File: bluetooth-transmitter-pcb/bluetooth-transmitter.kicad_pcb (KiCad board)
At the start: 2 copper layers, 16 parts, among them J1 Boot option, J2 Flash UART, SW1 Reset, SW2 RotaryEncoder_Switch, U1 ESP32-WROOM-32

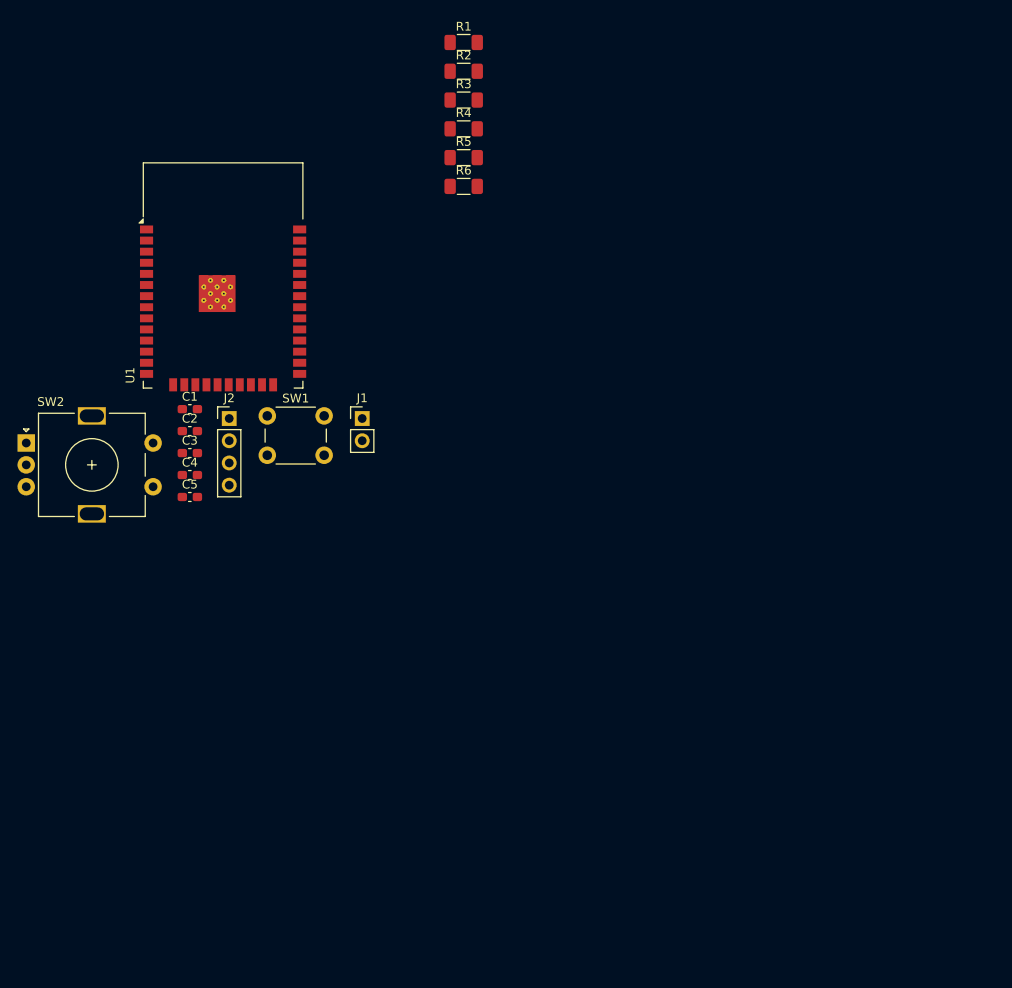
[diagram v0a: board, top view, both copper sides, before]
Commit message: Update PCB to last version
Add power chain and PCM1808 to schematic. Create PCB from shecmatic.
Make PCB ready for production.
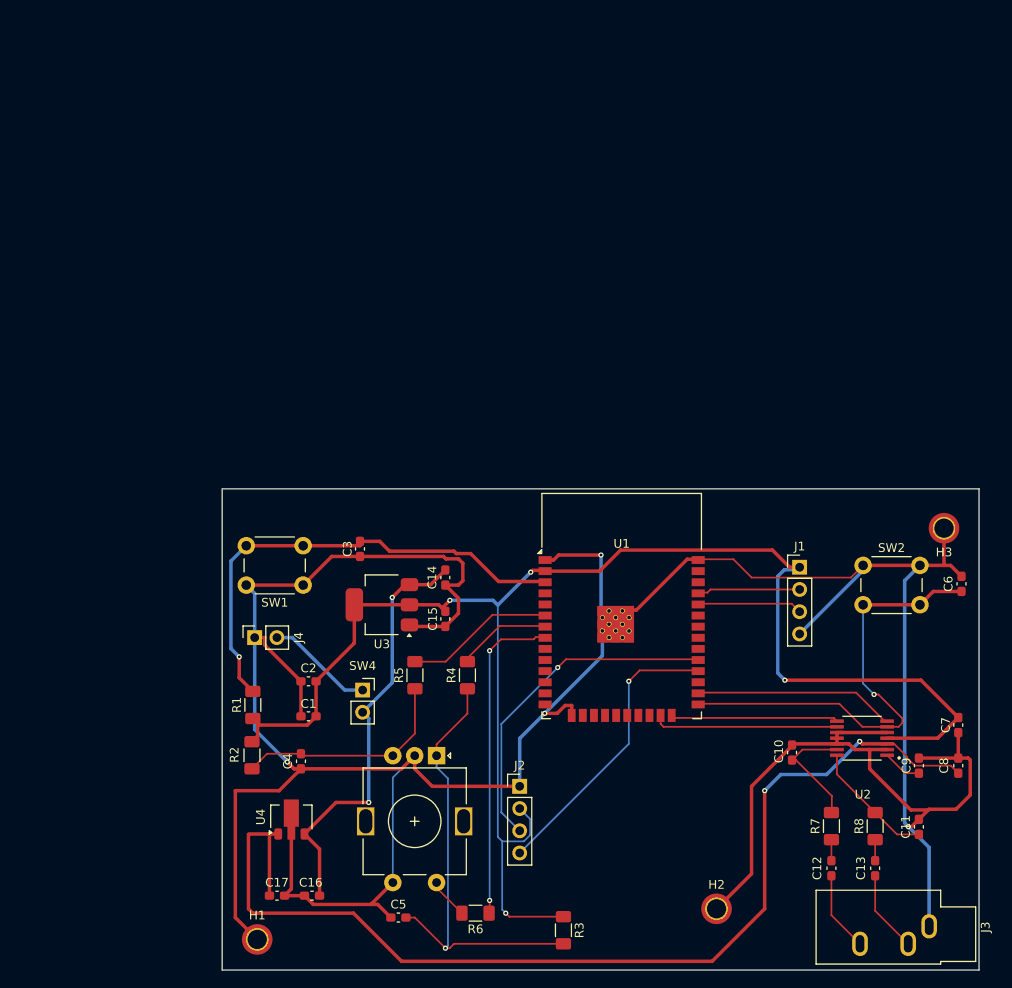
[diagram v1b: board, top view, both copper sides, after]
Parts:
- added C10: 2200pF, Capacitor_SMD:C_0603_1608Metric_Pad1.08x0.95mm_HandSolder, F.Cu at (128.6, 99.1)
- added C11: 2200pF, Capacitor_SMD:C_0603_1608Metric_Pad1.08x0.95mm_HandSolder, F.Cu at (143.1, 107.6)
- added C12: 2.2uF, Capacitor_SMD:C_0603_1608Metric_Pad1.08x0.95mm_HandSolder, F.Cu at (133.1, 112.4)
- added C13: 2.2uF, Capacitor_SMD:C_0603_1608Metric_Pad1.08x0.95mm_HandSolder, F.Cu at (138.1, 112.4)
- added C14: 1uF, Capacitor_SMD:C_0603_1608Metric_Pad1.08x0.95mm_HandSolder, F.Cu at (89.0, 79.1)
- added C15: 1uF, Capacitor_SMD:C_0603_1608Metric_Pad1.08x0.95mm_HandSolder, F.Cu at (89.0, 83.9)
- added C16: 0.1uF, Capacitor_SMD:C_0603_1608Metric_Pad1.08x0.95mm_HandSolder, F.Cu at (73.8, 115.5)
- added C17: 0.1uF, Capacitor_SMD:C_0603_1608Metric_Pad1.08x0.95mm_HandSolder, F.Cu at (69.8, 115.5)
- added C6: 1uF, Capacitor_SMD:C_0603_1608Metric_Pad1.08x0.95mm_HandSolder, F.Cu at (148.0, 79.9)
- added C7: 2.2uF, Capacitor_SMD:C_0603_1608Metric_Pad1.08x0.95mm_HandSolder, F.Cu at (147.6, 96.0)
- added C8: 2.2uF, Capacitor_SMD:C_0603_1608Metric_Pad1.08x0.95mm_HandSolder, F.Cu at (147.6, 100.6)
- added C9: 2.2uF, Capacitor_SMD:C_0603_1608Metric_Pad1.08x0.95mm_HandSolder, F.Cu at (143.1, 100.6)
- added H1: MountingHole_Pad, MountingHole:MountingHole_2.2mm_M2_ISO7380_Pad_TopOnly, F.Cu at (67.5, 120.5)
- added H2: MountingHole_Pad, MountingHole:MountingHole_2.2mm_M2_ISO7380_Pad_TopOnly, F.Cu at (120.0, 117.0)
- added H3: MountingHole_Pad, MountingHole:MountingHole_2.2mm_M2_ISO7380_Pad_TopOnly, F.Cu at (146.0, 73.5)
- added J3: AudioJack3, Connector_Audio:Jack_3.5mm_CUI_SJ1-3533NG_Horizontal, F.Cu at (144.3, 119.0)
- added J4: Power, Connector_PinSocket_2.54mm:PinSocket_1x02_P2.54mm_Vertical, F.Cu at (67.2, 86.0)
- added R7: 470, Resistor_SMD:R_1206_3216Metric_Pad1.30x1.75mm_HandSolder, F.Cu at (133.1, 107.5)
- added R8: 470, Resistor_SMD:R_1206_3216Metric_Pad1.30x1.75mm_HandSolder, F.Cu at (138.1, 107.5)
- added SW3: RotaryEncoder_Switch, Rotary_Encoder:RotaryEncoder_Alps_EC11E-Switch_Vertical_H20mm, F.Cu at (88.0, 99.5)
- added SW4: Power switch, Connector_PinSocket_2.54mm:PinSocket_1x02_P2.54mm_Vertical, F.Cu at (79.5, 92.0)
- added U2: PCM1808PWR, PCM1808:SOP65P640X120-14N, F.Cu at (136.6, 97.5)
- added U3: ADP3338AKCZ-3.3, Package_TO_SOT_SMD:SOT-223-3_TabPin2, F.Cu at (81.8, 82.2)
- added U4: L78L05_SOT89, Package_TO_SOT_SMD:SOT-89-3, F.Cu at (71.4, 106.5)
- C4: value 100nF -> 0.1unF
- C5: value 100nF -> 0.1uF
- J1: value Boot option -> Flash UART; footprint Connector_PinHeader_2.54mm:PinHeader_1x02_P2.54mm_Vertical -> Connector_PinHeader_2.54mm:PinHeader_1x04_P2.54mm_Vertical
- J2: value Flash UART -> OLED I2C
- R5, R6: value 1k -> 10k
- SW2: value RotaryEncoder_Switch -> Boot; footprint Rotary_Encoder:RotaryEncoder_Alps_EC11E-Switch_Vertical_H20mm -> Button_Switch_THT:SW_PUSH_6mm_H4.3mm
- moved SW2 96.7 mm to (136.8, 77.8)
- moved R3 95.6 mm to (102.5, 119.5), turned to -90 degrees
- moved R6 83.1 mm to (92.5, 117.5), turned to 180 degrees
- moved R2 81.8 mm to (66.9, 99.5), turned to -90 degrees
- moved R1 79.5 mm to (67.0, 93.7), turned to 90 degrees
- moved R4 62.5 mm to (91.5, 90.3), turned to 90 degrees
- moved R5 59.4 mm to (85.5, 90.3), turned to 90 degrees
- moved U1 59.2 mm to (109.2, 85.4)
- moved C5 53.7 mm to (83.6, 118.0), turned to 180 degrees
- moved J2 53.6 mm to (97.5, 103.0)
- moved J1 52.8 mm to (129.5, 78.0)
- moved C1 37.6 mm to (73.4, 95.0)
- moved C4 35.1 mm to (72.5, 100.1), turned to -90 degrees
- moved C2 31.7 mm to (73.4, 91.0), turned to 180 degrees
- moved C3 22.3 mm to (79.2, 75.9), turned to 90 degrees
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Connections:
- net Net-(U1-EN) renamed /EN
- C4 pad 1: Net-(U1-IO34) -> Net-(C4-Pad1)
- C5 pad 1: Net-(U1-IO35) -> Net-(C5-Pad1)
- J1 pad 1: Net-(J1-Pin_1) -> +3.3V
- J1 pad 2: GND -> /TX0
- J2 pad 1: +3.3V -> GND
- J2 pad 2: Net-(J2-Pin_2) -> +3.3V
- J2 pad 3: Net-(J2-Pin_3) -> /IO5
- J2 pad 4: GND -> /IO17
- R2 pad 2: Net-(U1-IO35) -> Net-(C4-Pad1)
- R3 pad 2: Net-(U1-IO34) -> Net-(C5-Pad1)
- R4 pad 1: +3.3V -> Net-(C5-Pad1)
- R4 pad 2: Net-(U1-IO33) -> /IO35
- R5 pad 1: Net-(R5-Pad1) -> Net-(C4-Pad1)
- R5 pad 2: Net-(U1-IO34) -> /IO34
- R6 pad 1: Net-(R6-Pad1) -> /IO32
- R6 pad 2: Net-(U1-IO35) -> Net-(R6-Pad2)
- U1 pad 23: unconnected-(U1-IO15-Pad23) -> /IO15
- U1 pad 24: unconnected-(U1-IO2-Pad24) -> /IO2
- U1 pad 25: Net-(J1-Pin_1) -> /IO0
- U1 pad 26: unconnected-(U1-IO4-Pad26) -> /IO4
- U1 pad 28: unconnected-(U1-IO17-Pad28) -> /IO17
- U1 pad 29: unconnected-(U1-IO5-Pad29) -> /IO5
- U1 pad 34: Net-(J2-Pin_3) -> /RX0
- U1 pad 35: Net-(J2-Pin_2) -> /TX0
- U1 pad 6: Net-(U1-IO34) -> /IO34
- U1 pad 7: Net-(U1-IO35) -> /IO35
- U1 pad 8: unconnected-(U1-IO32-Pad8) -> /IO32
- U1 pad 9: Net-(U1-IO33) -> unconnected-(U1-IO33-Pad9)
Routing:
- net GND: track 0.00 -> 405.0 mm, vias 0 -> 4
- net +3.3V: track 0.00 -> 175.7 mm, vias 0 -> 4
- net +5V: track 0.00 -> 123.5 mm, vias 0 -> 2
- net /EN: track 0.00 -> 55.0 mm, vias 0 -> 1
- net /IO0: track 0.00 -> 52.2 mm, vias 0 -> 1
- net Net-(C5-Pad1): track 0.00 -> 51.4 mm, vias 0 -> 1
- net /INV: track 0.00 -> 49.1 mm, vias 0 -> 2
- net /IO5: track 0.00 -> 38.6 mm, vias 0 -> 1
- net /IO32: track 0.00 -> 37.0 mm, vias 0 -> 2
- net /IO17: track 0.00 -> 33.2 mm, vias 0 -> 1
- net Net-(C4-Pad1): track 0.00 -> 25.6 mm
- net /IO4: track 0.00 -> 22.9 mm
- net /IO15: track 0.00 -> 21.3 mm
- net /IO2: track 0.00 -> 19.2 mm
- net /IO34: track 0.00 -> 17.1 mm
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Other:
- board outline added: 86.5 x 55 mm
